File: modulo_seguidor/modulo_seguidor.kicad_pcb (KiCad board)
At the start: 12 copper layers, 100 x 50 mm, 12 parts, among them J1 Battery, J4 Motor Izquierdo, J5 Motor Derecho, J6 puerto sensores, SW1 SW_Push, U1 LM7806_TO220

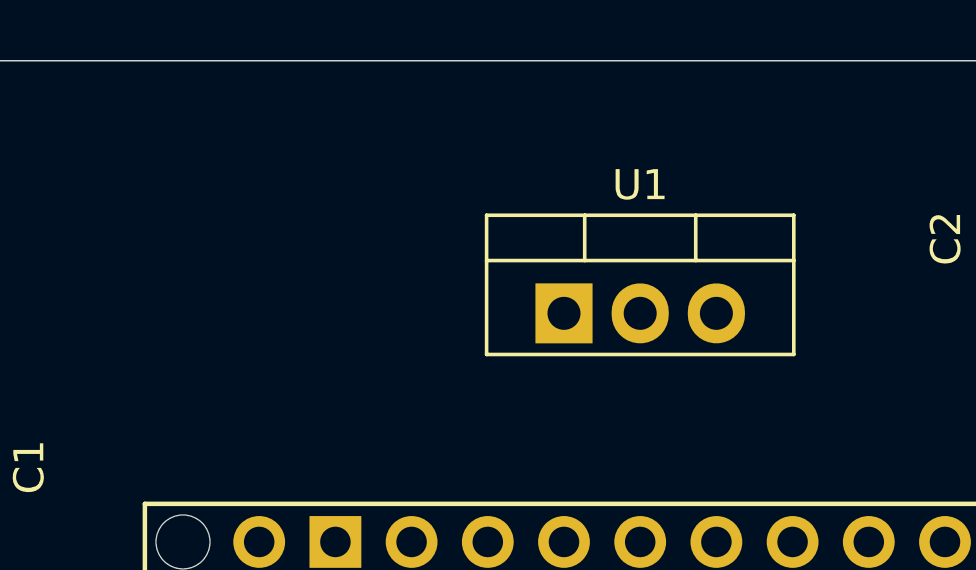
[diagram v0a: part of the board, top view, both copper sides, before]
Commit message: docs: Agrego TODOs, previews y documento la placa del modulo_seguidor
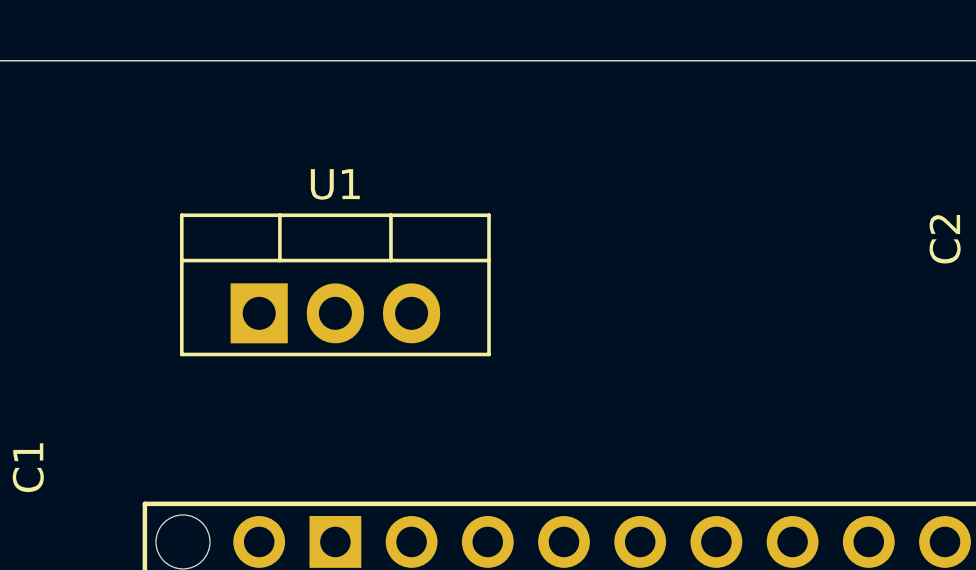
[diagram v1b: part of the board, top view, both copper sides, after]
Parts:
- moved U1 10.2 mm to (81.3, 58.4)
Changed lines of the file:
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@@
 	(footprint "Package_TO_SOT_THT:TO-220-3_Vertical"
 		(layer "F.Cu")
-		(at 91.44 58.42)
+		(at 81.28 58.42)
 		(descr "TO-220-3, Vertical, RM 2.54mm, see https://www.vishay.com/docs/66542/to-220-1.pdf")
 		(tags "TO-220-3 Vertical RM 2.54mm")

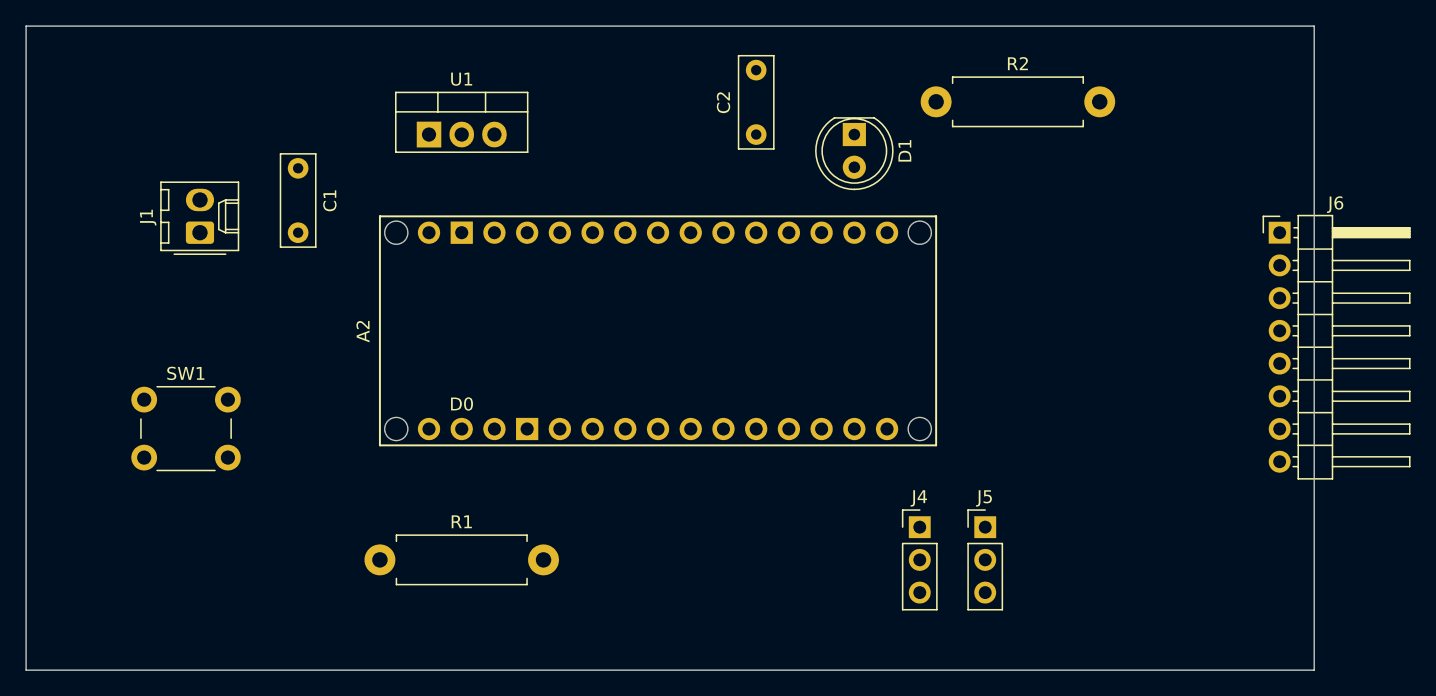
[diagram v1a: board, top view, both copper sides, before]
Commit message: feat: Agrego los cables en la pcb del modulo seguidor
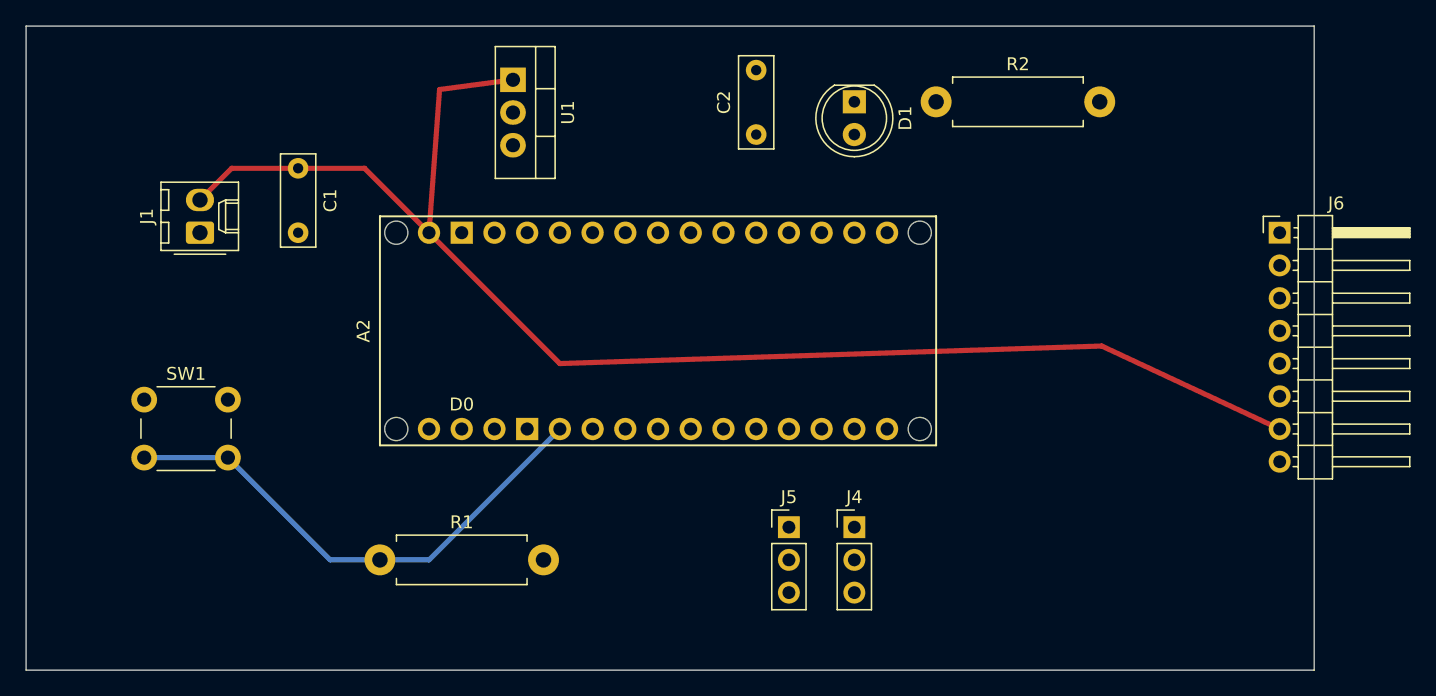
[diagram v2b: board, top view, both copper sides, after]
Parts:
- moved J5 15.2 mm to (109.2, 88.9)
- moved U1 7.78 mm to (87.8, 54.2), turned to -90 degrees
- moved J4 5.08 mm to (114.3, 88.9)
- moved D1 2.54 mm to (114.3, 55.9)
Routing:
- net GND: track 0.00 -> 179.7 mm
- net VCC: track 0.00 -> 109.5 mm
- net /Salida Regulador: track 0.00 -> 83.5 mm
- net /Sensor6: track 0.00 -> 60.0 mm
- net /Sensor5: track 0.00 -> 56.4 mm
- net /Sensor4: track 0.00 -> 52.6 mm
- net /Sensor3: track 0.00 -> 48.4 mm
- net /Sensor2: track 0.00 -> 45.3 mm
- net /Sensor1: track 0.00 -> 41.7 mm
- net /Boton_encendido: track 0.00 -> 39.8 mm
- net +5V: track 0.00 -> 35.1 mm
- net Net-(D1-A): track 0.00 -> 24.7 mm
- net /PWM_IZQ: track 0.00 -> 8.67 mm
- net /PWM_DER: track 0.00 -> 7.62 mm
- net Net-(D1-K): track 0.00 -> 6.35 mm

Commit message: refactor: Reordeno la pcb del modulo seguidor y sus conexiones
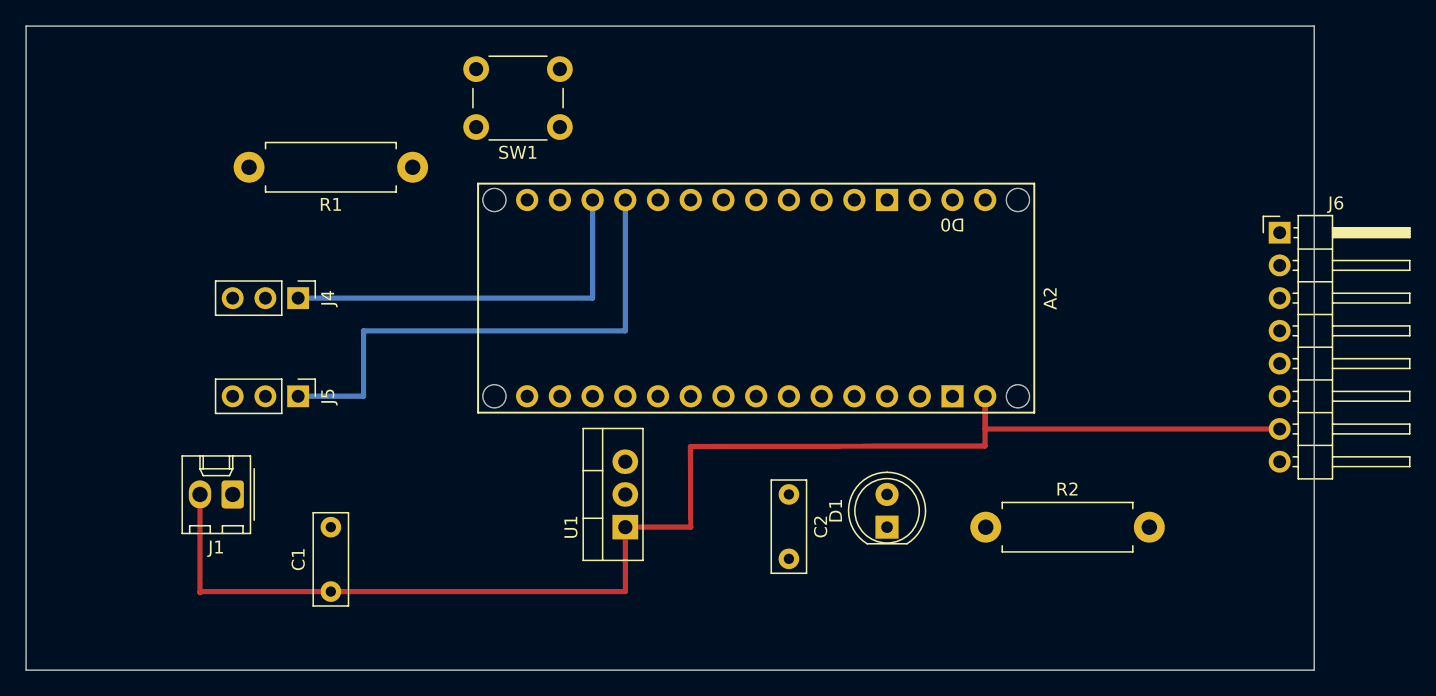
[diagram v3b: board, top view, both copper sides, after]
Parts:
- moved J4 46.7 mm to (71.1, 71.1), turned to -90 degrees
- moved J5 39.4 mm to (71.1, 78.7), turned to -90 degrees
- moved SW1 38.6 mm to (91.4, 57.8), turned to 180 degrees
- moved U1 35.8 mm to (96.5, 88.9), turned to 90 degrees
- moved A2 35.7 mm to (85.1, 71.1), turned to -90 degrees
- moved R2 33.2 mm to (124.5, 88.9)
- moved D1 33.1 mm to (116.8, 88.9), turned to 90 degrees
- moved C1 33.0 mm to (73.7, 93.9), turned to 90 degrees
- moved R1 30.6 mm to (80.0, 61.0), turned to 180 degrees
- moved C2 28.1 mm to (109.2, 86.4), turned to -90 degrees
- moved J1 20.5 mm to (66.0, 86.4), turned to 180 degrees
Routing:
- net /PWM_DER: track 7.62 -> 40.6 mm
- net /Salida Regulador: track 83.5 -> 55.9 mm
- net +5V: track 35.1 -> 60.9 mm
- net /Sensor6: track 60.0 -> 36.6 mm
- net /PWM_IZQ: track 8.67 -> 30.5 mm
- net /Sensor1: track 41.7 -> 58.7 mm
- net /Sensor5: track 56.4 -> 40.1 mm
- net Net-(D1-A): track 24.7 -> 10.2 mm
- net /Sensor4: track 52.6 -> 43.3 mm
- net /Sensor2: track 45.3 -> 49.7 mm
- net /Boton_encendido: track 39.8 -> 43.2 mm
- net /Sensor3: track 48.4 -> 46.7 mm
- net Net-(D1-K): track 6.35 -> 7.66 mm
- net GND: track 179.7 -> 178.9 mm

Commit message: refactor: Hago las conexiones n poco más cortas y rectas
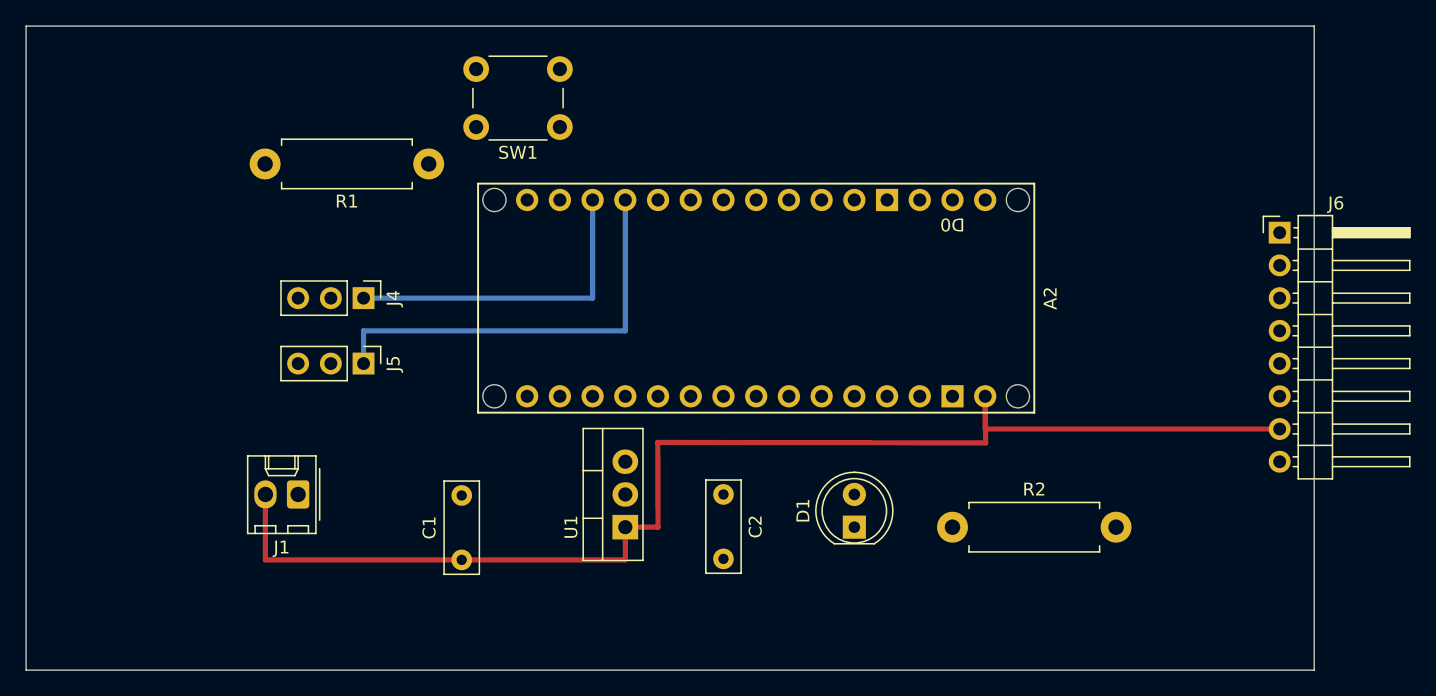
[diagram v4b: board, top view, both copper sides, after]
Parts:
- moved C1 10.5 mm to (83.8, 91.4)
- moved J5 5.68 mm to (76.2, 76.2)
- moved C2 5.08 mm to (104.1, 86.4)
- moved J1 5.08 mm to (71.1, 86.4)
- moved J4 5.08 mm to (76.2, 71.1)
- moved R2 2.58 mm to (121.9, 88.9)
- moved D1 2.54 mm to (114.3, 88.9)
- moved R1 1.27 mm to (81.3, 60.7)
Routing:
- net /Salida Regulador: track 55.9 -> 45.7 mm
- net VCC: track 109.1 -> 99.2 mm
- net /PWM_DER: track 40.6 -> 33.0 mm
- net /PWM_IZQ: track 30.5 -> 25.4 mm
- net /Sensor2: track 49.7 -> 54.1 mm
- net GND: track 178.9 -> 174.9 mm
- net /Sensor3: track 46.7 -> 50.1 mm
- net /Sensor4: track 43.3 -> 46.1 mm
- net Net-(D1-A): track 10.2 -> 7.62 mm
- net /Sensor5: track 40.1 -> 42.3 mm
- net /Sensor6: track 36.6 -> 38.1 mm
- net /Boton_encendido: track 43.2 -> 44.6 mm
- net /Sensor1: track 58.7 -> 58.0 mm
